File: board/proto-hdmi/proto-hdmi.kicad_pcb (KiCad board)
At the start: 2 copper layers, 30.5 x 30.5 mm, 2 parts, among them J1 Conn_02x12_Odd_Even, J2 HDMI_A_1.4

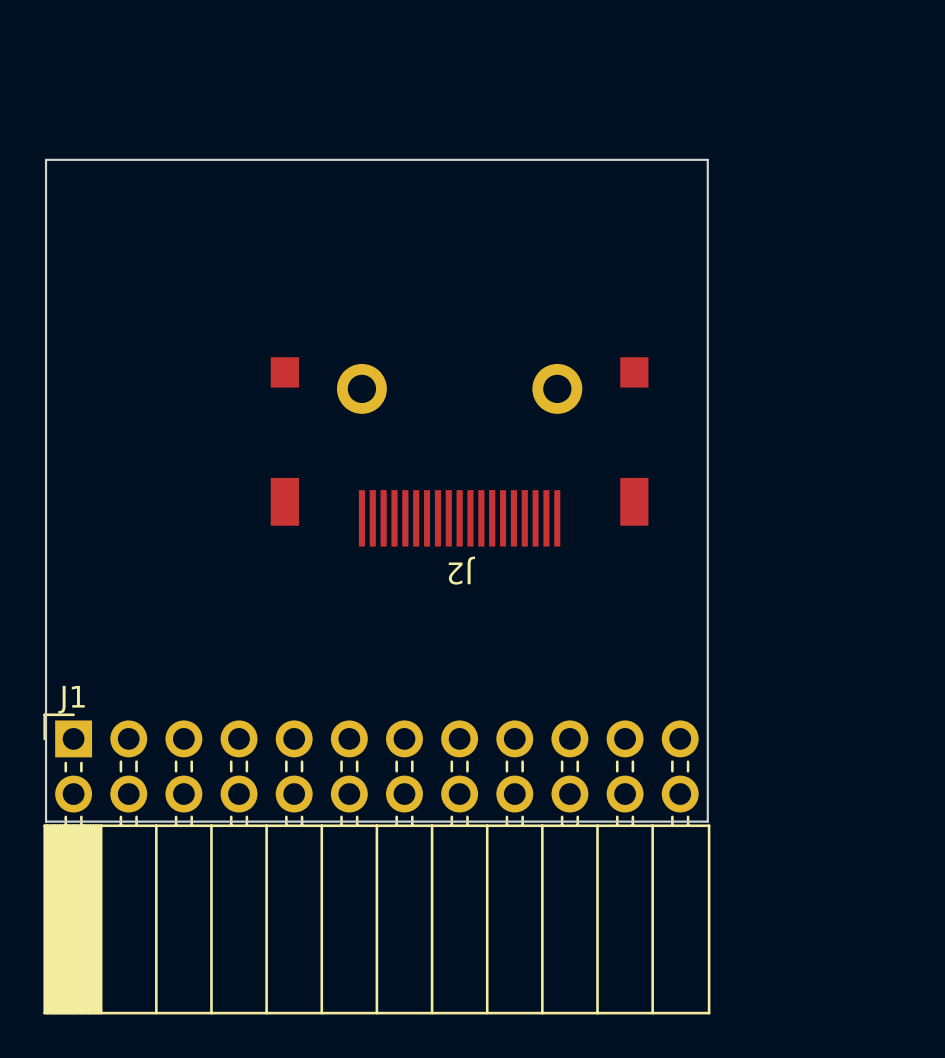
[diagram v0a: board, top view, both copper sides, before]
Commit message: Route HDMI in resistor networks.
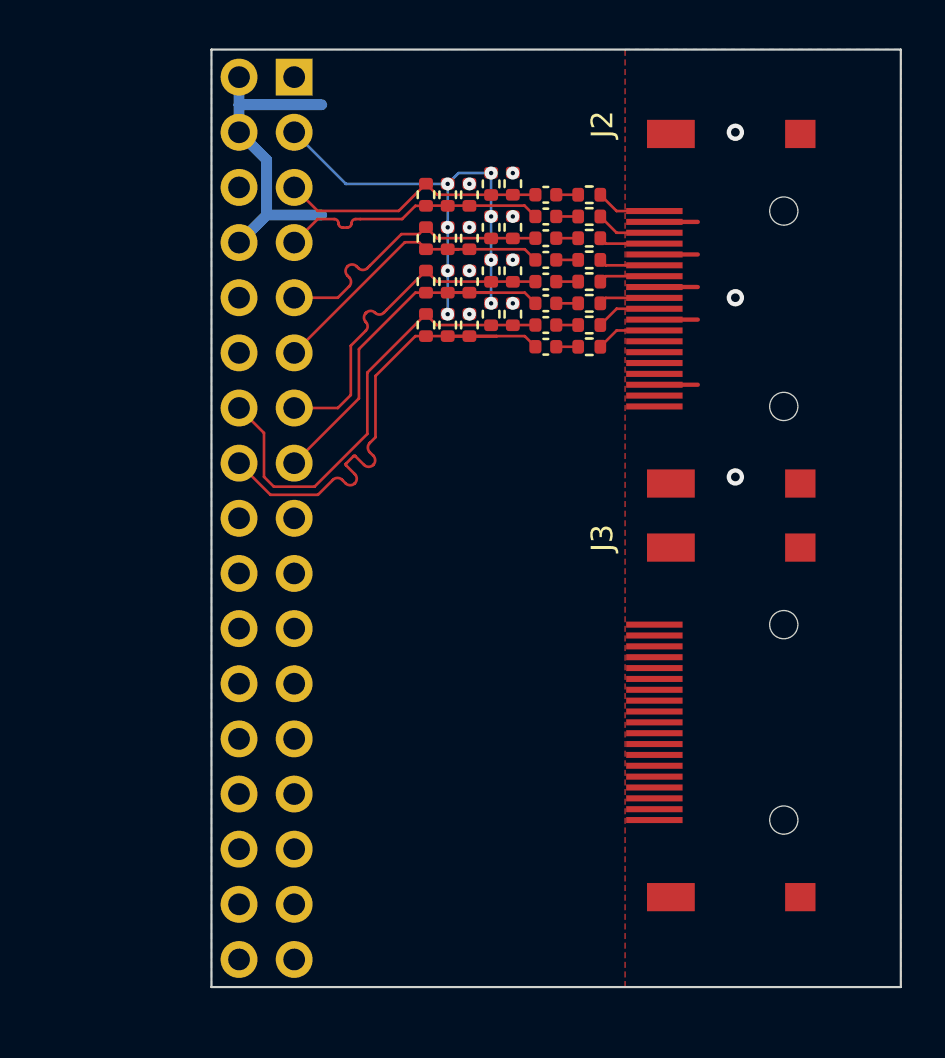
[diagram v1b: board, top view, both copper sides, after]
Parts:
- added C1: C, Capacitor_SMD:C_0402_1005Metric, F.Cu at (148.8, 96.9)
- added C2: C, Capacitor_SMD:C_0402_1005Metric, F.Cu at (148.8, 97.9)
- added C3: C, Capacitor_SMD:C_0402_1005Metric, F.Cu at (148.8, 100.9)
- added C4: C, Capacitor_SMD:C_0402_1005Metric, F.Cu at (148.8, 101.9)
- added C5: C, Capacitor_SMD:C_0402_1005Metric, F.Cu at (148.8, 98.9)
- added C6: C, Capacitor_SMD:C_0402_1005Metric, F.Cu at (148.8, 99.9)
- added C7: C, Capacitor_SMD:C_0402_1005Metric, F.Cu at (148.8, 102.9)
- added C8: C, Capacitor_SMD:C_0402_1005Metric, F.Cu at (148.8, 103.9)
- added J3: HDMI_A_1.4, 0Local:CNC_2000-1-2-41-00-BK, F.Cu at (153.8, 121.2)
- added R1: 50R, Resistor_SMD:R_0402_1005Metric, F.Cu at (150.8, 96.9)
- added R10: 82R, Resistor_SMD:R_0402_1005Metric, F.Cu at (147.2, 100.4)
- added R11: 150R, Resistor_SMD:R_0402_1005Metric, F.Cu at (146.2, 96.4)
- added R12: 150R, Resistor_SMD:R_0402_1005Metric, F.Cu at (146.2, 100.4)
- added R13: 82R, Resistor_SMD:R_0402_1005Metric, F.Cu at (145.2, 96.9)
- added R14: 82R, Resistor_SMD:R_0402_1005Metric, F.Cu at (145.2, 100.9)
- added R15: 150R, Resistor_SMD:R_0402_1005Metric, F.Cu at (144.2, 96.9)
- added R16: 150R, Resistor_SMD:R_0402_1005Metric, F.Cu at (144.2, 100.9)
- added R17: 82R, Resistor_SMD:R_0402_1005Metric, F.Cu at (147.2, 98.4)
- added R18: 82R, Resistor_SMD:R_0402_1005Metric, F.Cu at (147.2, 102.4)
- added R19: 150R, Resistor_SMD:R_0402_1005Metric, F.Cu at (146.2, 98.4)
- added R2: 50R, Resistor_SMD:R_0402_1005Metric, F.Cu at (150.8, 97.9)
- added R20: 150R, Resistor_SMD:R_0402_1005Metric, F.Cu at (146.2, 102.4)
- added R21: 100R, Resistor_SMD:R_0402_1005Metric, F.Cu at (143.2, 96.9)
- added R22: 100R, Resistor_SMD:R_0402_1005Metric, F.Cu at (143.2, 100.9)
- added R23: 82R, Resistor_SMD:R_0402_1005Metric, F.Cu at (145.2, 98.9)
- added R24: 82R, Resistor_SMD:R_0402_1005Metric, F.Cu at (145.2, 102.9)
- added R25: 150R, Resistor_SMD:R_0402_1005Metric, F.Cu at (144.2, 98.9)
- added R26: 150R, Resistor_SMD:R_0402_1005Metric, F.Cu at (144.2, 102.9)
- added R27: 100R, Resistor_SMD:R_0402_1005Metric, F.Cu at (143.2, 98.9)
- added R28: 100R, Resistor_SMD:R_0402_1005Metric, F.Cu at (143.2, 102.9)
- added R3: 50R, Resistor_SMD:R_0402_1005Metric, F.Cu at (150.8, 100.9)
- added R4: 50R, Resistor_SMD:R_0402_1005Metric, F.Cu at (150.8, 101.9)
- added R5: 50R, Resistor_SMD:R_0402_1005Metric, F.Cu at (150.8, 98.9)
- added R6: 50R, Resistor_SMD:R_0402_1005Metric, F.Cu at (150.8, 99.9)
- added R7: 50R, Resistor_SMD:R_0402_1005Metric, F.Cu at (150.8, 102.9)
- added R8: 50R, Resistor_SMD:R_0402_1005Metric, F.Cu at (150.8, 103.9)
- added R9: 82R, Resistor_SMD:R_0402_1005Metric, F.Cu at (147.2, 96.3)
- J1: value Conn_02x12_Odd_Even -> Conn_02x17_Odd_Even; footprint Connector_PinSocket_2.54mm:PinSocket_2x12_P2.54mm_Horizontal -> Connector_PinSocket_2.54mm:PinSocket_2x17_P2.54mm_Horizontal
- moved J1 32.1 mm to (137.2, 91.4), turned to 0 degrees
- moved J2 13.2 mm to (153.8, 102.1), turned to 90 degrees
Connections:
- J1 pad 1: unconnected-(J1-Pad1) -> +5V
- J1 pad 11: unconnected-(J1-Pad11) -> /LVDS_D1_N
- J1 pad 13: unconnected-(J1-Pad13) -> /LVDS_D0_P
- J1 pad 14: unconnected-(J1-Pad14) -> /LVDS_CK_P
- J1 pad 15: GND -> /LVDS_D0_N
- J1 pad 16: GND -> /LVDS_CK_N
- J1 pad 2: +2V5 -> GND
- J1 pad 23: GND -> unconnected-(J1-Pad23)
- J1 pad 24: GND -> unconnected-(J1-Pad24)
- J1 pad 3: unconnected-(J1-Pad3) -> +3V3
- J1 pad 4: unconnected-(J1-Pad4) -> GND
- J1 pad 5: unconnected-(J1-Pad5) -> /LVDS_D2_P
- J1 pad 7: GND -> /LVDS_D2_N
- J1 pad 9: unconnected-(J1-Pad9) -> /LVDS_D1_P
- J2 pad 1: unconnected-(J2-Pad1) -> /HDMI_D2_P
- J2 pad 10: unconnected-(J2-Pad10) -> /HDMI_CK_P
- J2 pad 12: unconnected-(J2-Pad12) -> /HDMI_CK_N
- J2 pad 3: unconnected-(J2-Pad3) -> /HDMI_D2_N
- J2 pad 4: unconnected-(J2-Pad4) -> /HDMI_D1_P
- J2 pad 6: unconnected-(J2-Pad6) -> /HDMI_D1_N
- J2 pad 7: unconnected-(J2-Pad7) -> /HDMI_D0_P
- J2 pad 9: unconnected-(J2-Pad9) -> /HDMI_D0_N
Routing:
- net GND: track 0.00 -> 25.1 mm, vias 0 -> 11
- net /LVDS_CK_N: track 0.00 -> 24.0 mm
- net +3V3: track 0.00 -> 22.3 mm, vias 0 -> 8
- net /LVDS_CK_P: track 0.00 -> 21.5 mm
- net /LVDS_D0_N: track 0.00 -> 17.9 mm
- net /LVDS_D0_P: track 0.00 -> 15.9 mm
- net /LVDS_D1_N: track 0.00 -> 14.0 mm
- net /LVDS_D1_P: track 0.00 -> 13.5 mm
- net /LVDS_D2_N: track 0.00 -> 12.4 mm
- net /LVDS_D2_P: track 0.00 -> 12.3 mm
- net /HDMI_D2_P: track 0.00 -> 2.80 mm
- net /HDMI_D2_N: track 0.00 -> 2.80 mm
- net /HDMI_CK_P: track 0.00 -> 2.80 mm
- net /HDMI_CK_N: track 0.00 -> 2.80 mm
- net /HDMI_D1_P: track 0.00 -> 2.59 mm
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- added copper zone on B.Cu, net GND
- added copper zone on F.Cu, net GND
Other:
- board size 30.5 x 30.5 mm -> 31.8 x 43.2 mm

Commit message: Remove extraneous LVDS termination resistors.
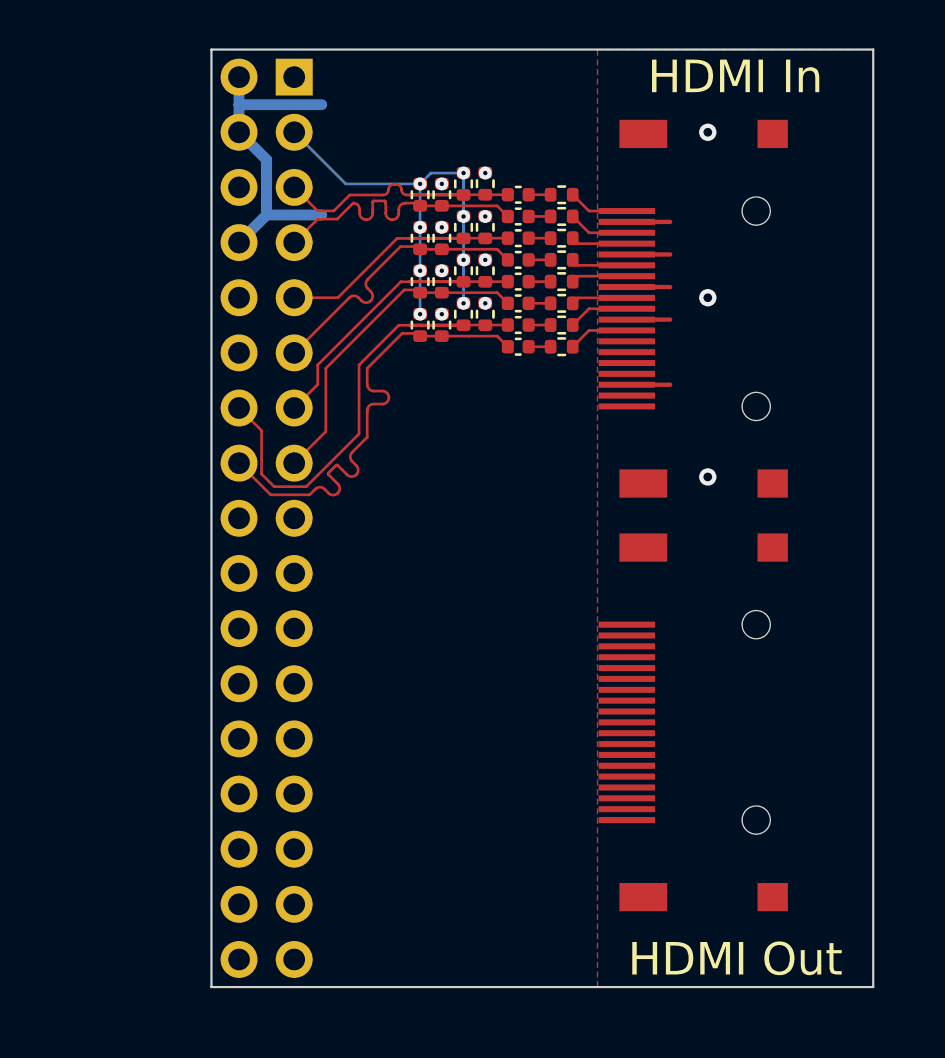
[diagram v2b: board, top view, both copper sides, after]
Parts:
- removed R21, R22, R27, R28: 100R, Resistor_SMD:R_0402_1005Metric
- moved C1 1.27 mm to (147.5, 96.9)
- moved C2 1.27 mm to (147.5, 97.9)
- moved C3 1.27 mm to (147.5, 100.9)
- moved C4 1.27 mm to (147.5, 101.9)
- moved C5 1.27 mm to (147.5, 98.9)
- moved C6 1.27 mm to (147.5, 99.9)
- moved C7 1.27 mm to (147.5, 102.9)
- moved C8 1.27 mm to (147.5, 103.9)
- moved J2 1.27 mm to (152.5, 102.1)
- moved J3 1.27 mm to (152.5, 121.2)
- moved R1 1.27 mm to (149.5, 96.9)
- moved R2 1.27 mm to (149.5, 97.9)
- moved R3 1.27 mm to (149.5, 100.9)
- moved R4 1.27 mm to (149.5, 101.9)
- moved R5 1.27 mm to (149.5, 98.9)
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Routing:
- net /LVDS_D0_N: track 17.9 -> 15.1 mm
- net /LVDS_CK_N: track 24.0 -> 22.4 mm
- net /LVDS_D2_P: track 12.3 -> 13.6 mm
- net +3V3: track 22.3 -> 21.1 mm
- net /LVDS_CK_P: track 21.5 -> 22.5 mm
- net /LVDS_D1_N: track 14.0 -> 13.2 mm
- net /LVDS_D2_N: track 12.4 -> 13.2 mm
- net /LVDS_D0_P: track 15.9 -> 15.3 mm
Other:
- board size 31.8 x 43.2 mm -> 30.5 x 43.2 mm
- board text added: "HDMI In"
- board text added: "HDMI Out"

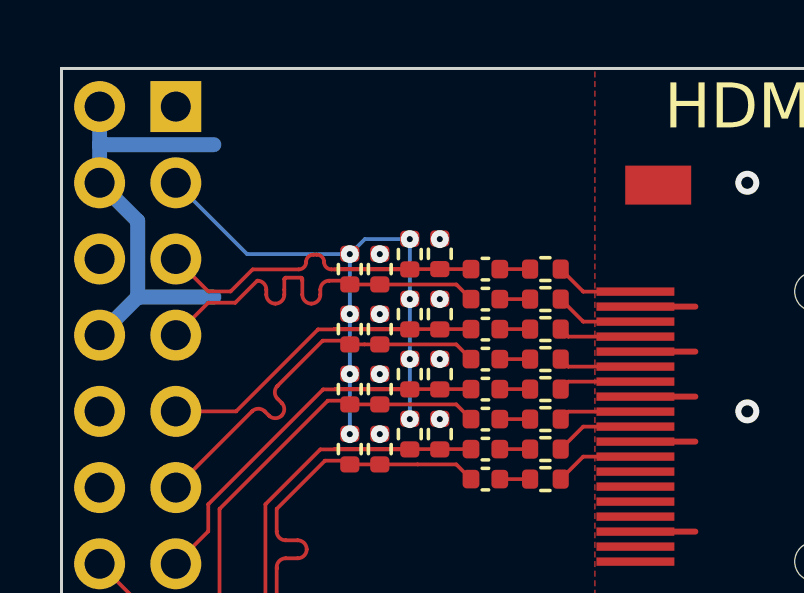
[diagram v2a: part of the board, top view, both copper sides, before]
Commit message: Add labels to HDMI board.
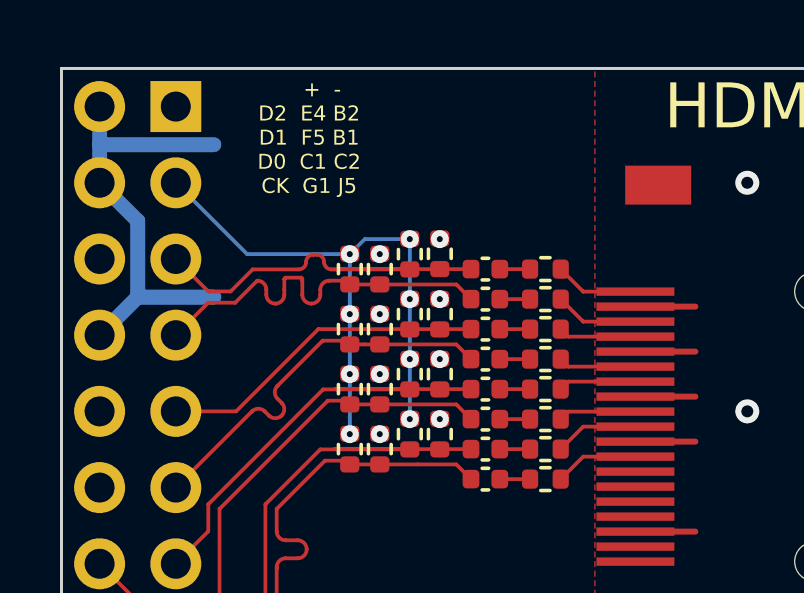
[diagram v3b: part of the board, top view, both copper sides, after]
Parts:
- added REF**: OSHW-Symbol_6.7x6mm_SilkScreen, Symbol:OSHW-Symbol_6.7x6mm_SilkScreen, B.Cu at (151.1, 100.3)
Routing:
- net /LVDS_D1_P: track 13.5 -> 11.0 mm
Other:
- board text added: "+ - D2 E4 B2 D1 F5 B1 D0 C1 C2 CK G1 J5"
- board text added: "HDMI Expansion v${REVISION}"
- board text added: "for Olimex iCE40HX8K-EVB https://github.com/Elemecca/1240pi licensed under CERN-OHL-P v2"
